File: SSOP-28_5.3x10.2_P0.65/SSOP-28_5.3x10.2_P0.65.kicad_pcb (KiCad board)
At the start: 2 copper layers, 17.8 x 35.6 mm, 6 parts, among them J101 Conn_01x26, J102 Conn_01x26, J103 Conn_01x26, J104 Conn_01x26, U101 SSOP-28

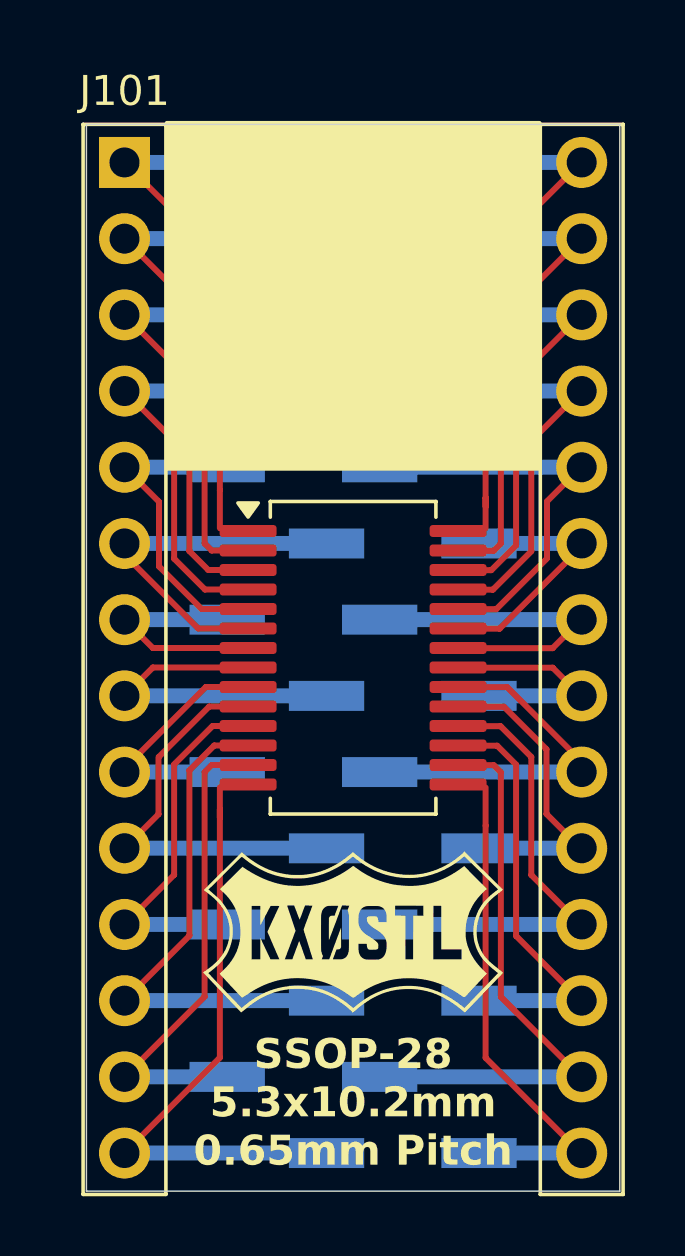
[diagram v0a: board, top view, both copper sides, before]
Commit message: Created SMDIP-16, QFP-48, QFP-32, QFN-80, QFN-68, QFN-64, QFN-60, QFN-56, QFN-48, QFN-36, QFN-28, QFN-20, QFP-32, QFP-48
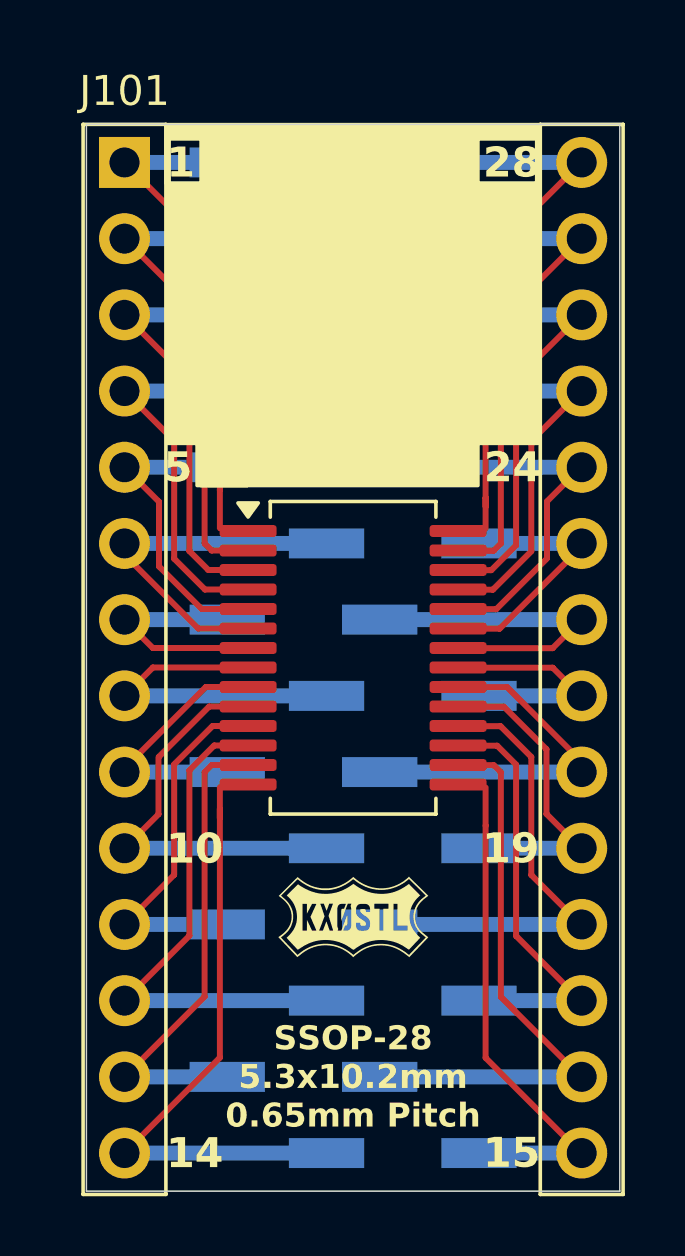
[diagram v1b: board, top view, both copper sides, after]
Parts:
- removed the G*** at (131.6, 112.3)
- added G***: LOGO, libraries:Logo_5mm_inv, F.Cu at (131.6, 111.8)
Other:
- board text added: "1"
- board text added: "10"
- board text added: "14"
- board text added: "15"
- board text added: "19"
- board text added: "24"
- board text added: "28"
- board text added: "5"
